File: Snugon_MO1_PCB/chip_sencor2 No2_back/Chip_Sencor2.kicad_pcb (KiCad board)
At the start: 2 copper layers, 32 x 58 mm, 7 parts, among them J2 Conn_01x8_Pin + 2, SW10 SW_PUSH, SW11 SW_PUSH, SW7 SW_PUSH, SW8 SW_PUSH, SW9 SW_PUSH

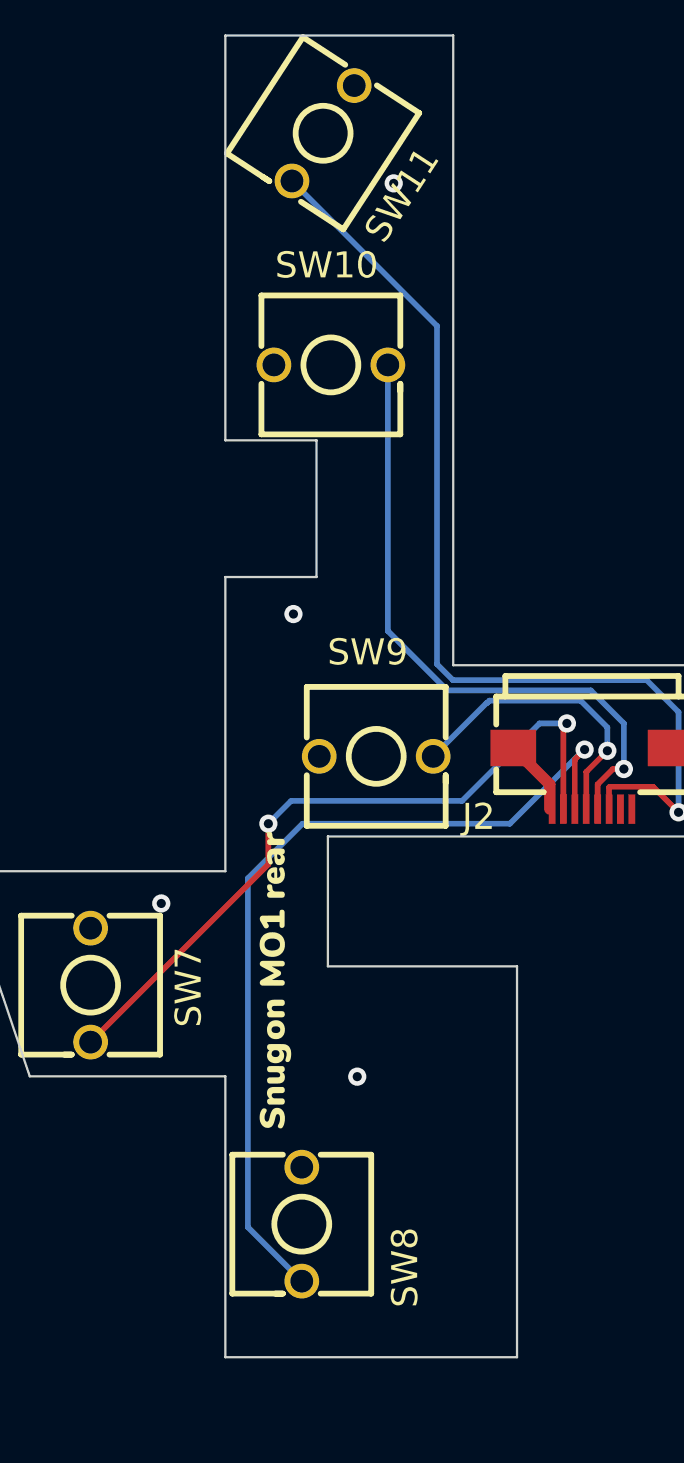
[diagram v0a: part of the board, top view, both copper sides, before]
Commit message: スイッチとエンコーダーはPCBAしない
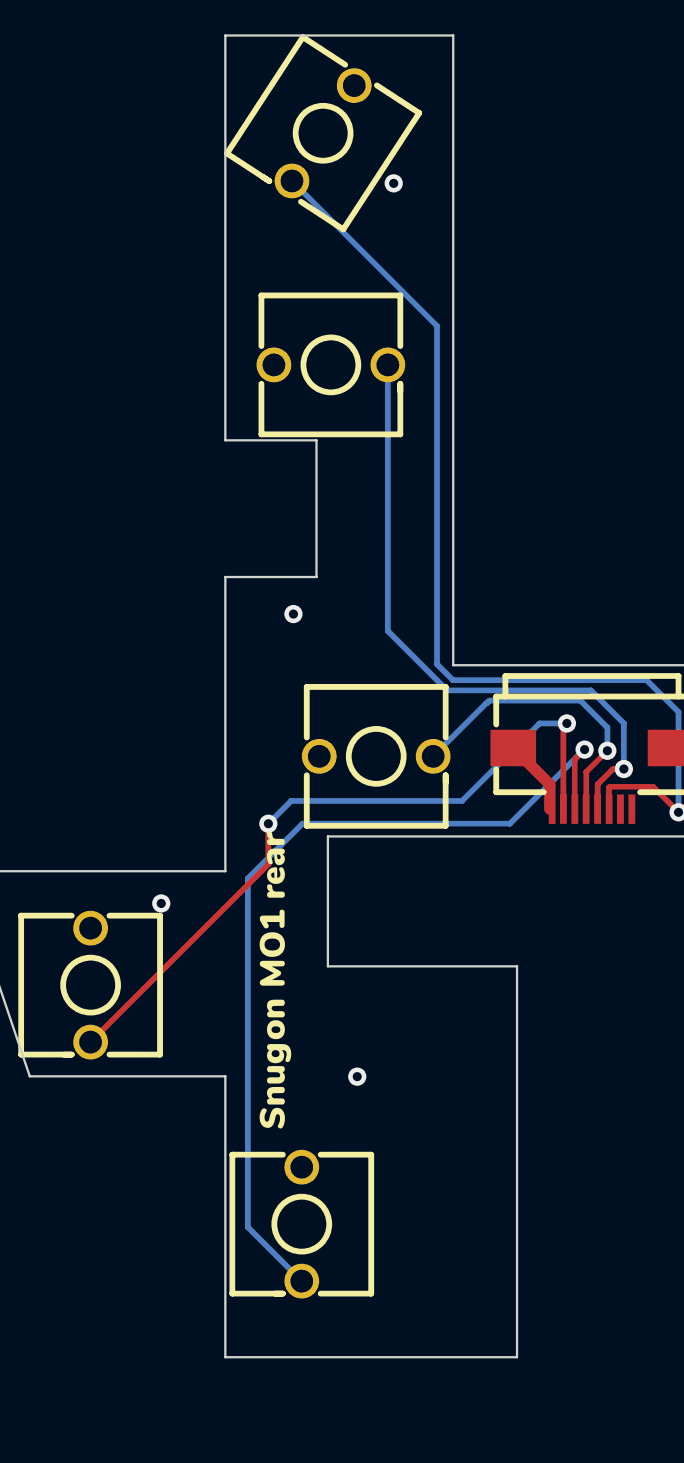
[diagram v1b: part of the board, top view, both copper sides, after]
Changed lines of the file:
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@@
   (footprint "0:SW-TH_L6.2-W6.2-P5.00" (layer "F.Cu")
     (at 114.243 78.567)
-    (property "LCSC" "C400268")
+    (property "LCSC" "")
     (property "Sheetfile" "Chip_Sencor2.kicad_sch")
     (property "Sheetname" "")
     (attr through_hole)
-    (fp_text reference "SW10" (at -2.455 -4.369) (layer "F.SilkS")
+    (fp_text reference "SW10" (at -2.455 -4.369) (layer "F.SilkS") hide
         (effects (font (size 1.143 1.143) (thickness 0.152)) (justify left))
     )
@@
   (footprint "0:SW-TH_L6.2-W6.2-P5.00" (layer "F.Cu")
     (at 112.966 116.273 -90)
-    (property "LCSC" "C400268")
+    (property "LCSC" "")
     (property "Sheetfile" "Chip_Sencor2.kicad_sch")
     (property "Sheetname" "")
     (attr through_hole)
-    (fp_text reference "SW8" (at 0.127 -4.534 90) (layer "F.SilkS")
+    (fp_text reference "SW8" (at 0.127 -4.534 90) (layer "F.SilkS") hide
         (effects (font (size 1.143 1.143) (thickness 0.152)) (justify right))
     )
@@
   (footprint "0:SW-TH_L6.2-W6.2-P5.00" (layer "F.Cu")
     (at 103.699 105.784 -90)
-    (property "LCSC" "C400268")
+    (property "LCSC" "")
     (property "Sheetfile" "Chip_Sencor2.kicad_sch")
     (property "Sheetname" "")
     (attr through_hole)
-    (fp_text reference "SW7" (at -1.684 -4.301 90) (layer "F.SilkS")
+    (fp_text reference "SW7" (at -1.684 -4.301 90) (layer "F.SilkS") hide
         (effects (font (size 1.143 1.143) (thickness 0.152)) (justify right))
     )
@@
   (footprint "0:SW-TH_L6.2-W6.2-P5.00" (layer "F.Cu")
     (at 116.233 95.745)
-    (property "LCSC" "C400268")
+    (property "LCSC" "")
     (property "Sheetfile" "Chip_Sencor2.kicad_sch")
     (property "Sheetname" "")
     (attr through_hole)
-    (fp_text reference "SW9" (at -2.145 -4.567) (layer "F.SilkS")
+    (fp_text reference "SW9" (at -2.145 -4.567) (layer "F.SilkS") hide
         (effects (font (size 1.143 1.143) (thickness 0.152)) (justify left))
     )
@@
     (property "ki_keywords" "connector")
     (attr smd)
-    (fp_text reference "J2" (at -5.7 1.6815) (layer "F.SilkS")
+    (fp_text reference "J2" (at -5.7 1.6815) (layer "F.SilkS") hide
         (effects (font (size 1.143 1.143) (thickness 0.152)) (justify left))
     )
@@
   (footprint "0:SW-TH_L6.2-W6.2-P5.00" (layer "F.Cu")
     (at 113.902 68.402 -123.125)
-    (property "LCSC" "C400268")
+    (property "LCSC" "")
     (property "Sheetfile" "Chip_Sencor2.kicad_sch")
     (property "Sheetname" "")
     (attr through_hole)
-    (fp_text reference "SW11" (at -1.898995 -4.370564 56.875) (layer "F.SilkS")
+    (fp_text reference "SW11" (at -1.898995 -4.370564 56.875) (layer "F.SilkS") hide
         (effects (font (size 1.143 1.143) (thickness 0.152)) (justify right))
     )
